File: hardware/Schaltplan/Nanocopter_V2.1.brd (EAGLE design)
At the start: 142 x 100 mm, 123 parts, among them IC1 CY7C68013A-56QFNLFXC, M1A TPSQTP20SQ, M1B TPSQTP20SQ, M1C TPSQTP20SQ, M2A TPSQTP20SQ, M2B TPSQTP20SQ, M2C TPSQTP20SQ, M3A TPSQTP20SQ, M3B TPSQTP20SQ, M3C TPSQTP20SQ, M4A TPSQTP20SQ, M4B TPSQTP20SQ, M4C TPSQTP20SQ, T5 IRLML2502, T6 IRLML2502, T7 IRLML2502, T8 IRLML2502, U2 PRTR5V0U2X, U3 LM3480-3.3, X1 USBSMD, X2 53261-08, X3 53261-06, X4 53261-03, X5 53261-03, X6 53261-06

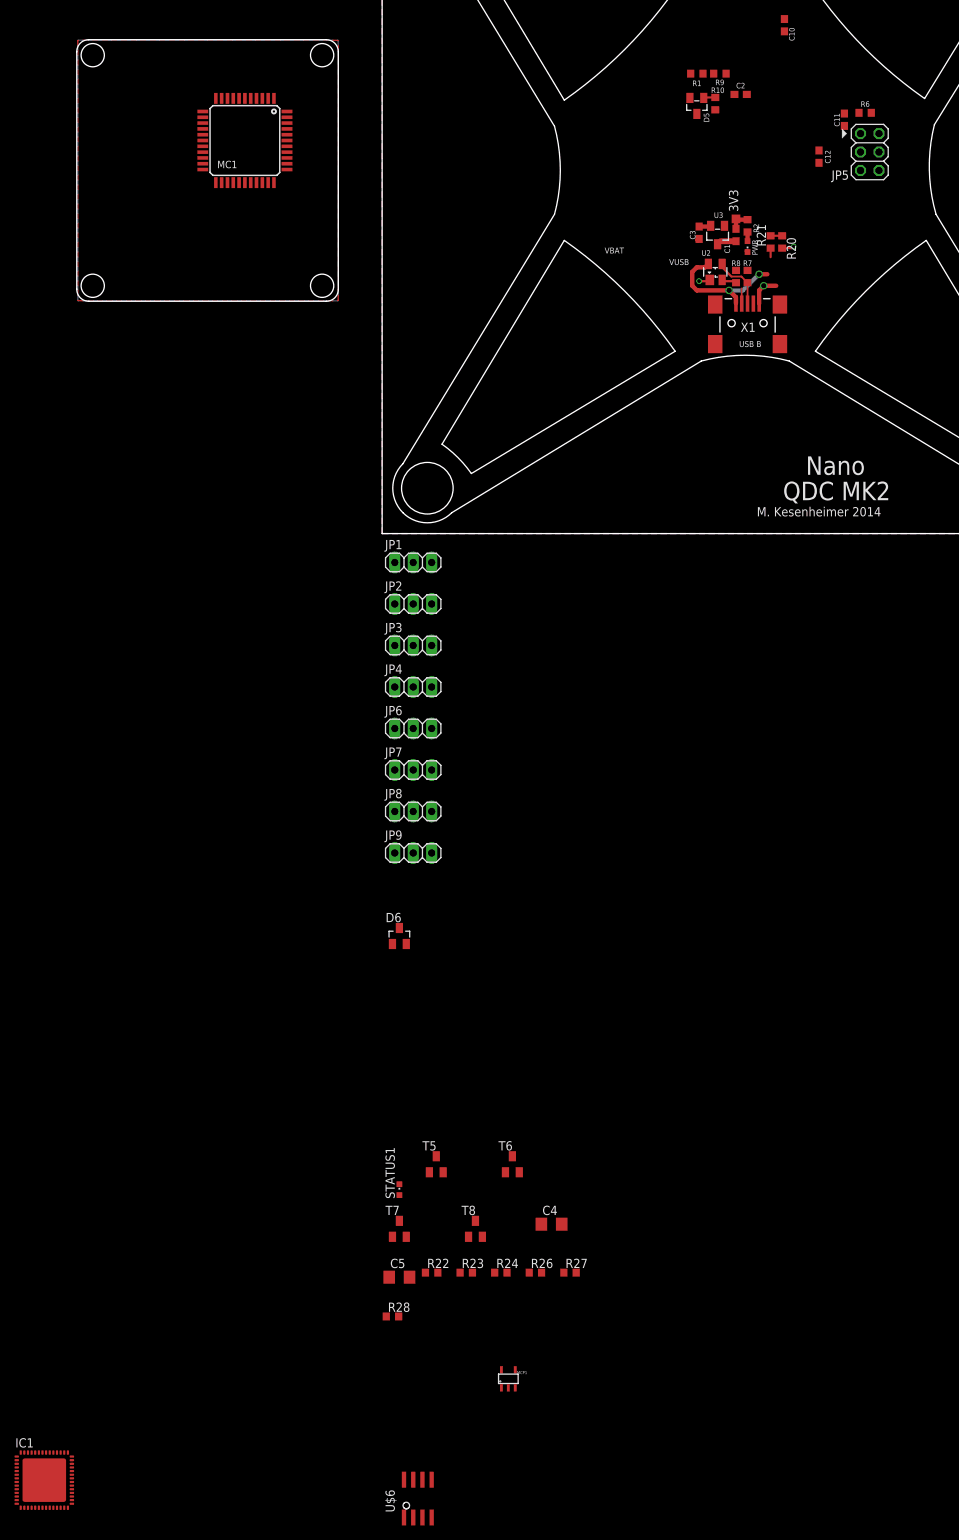
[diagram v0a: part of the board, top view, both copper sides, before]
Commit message: Dimensionen von SimpleControl aktualisiert
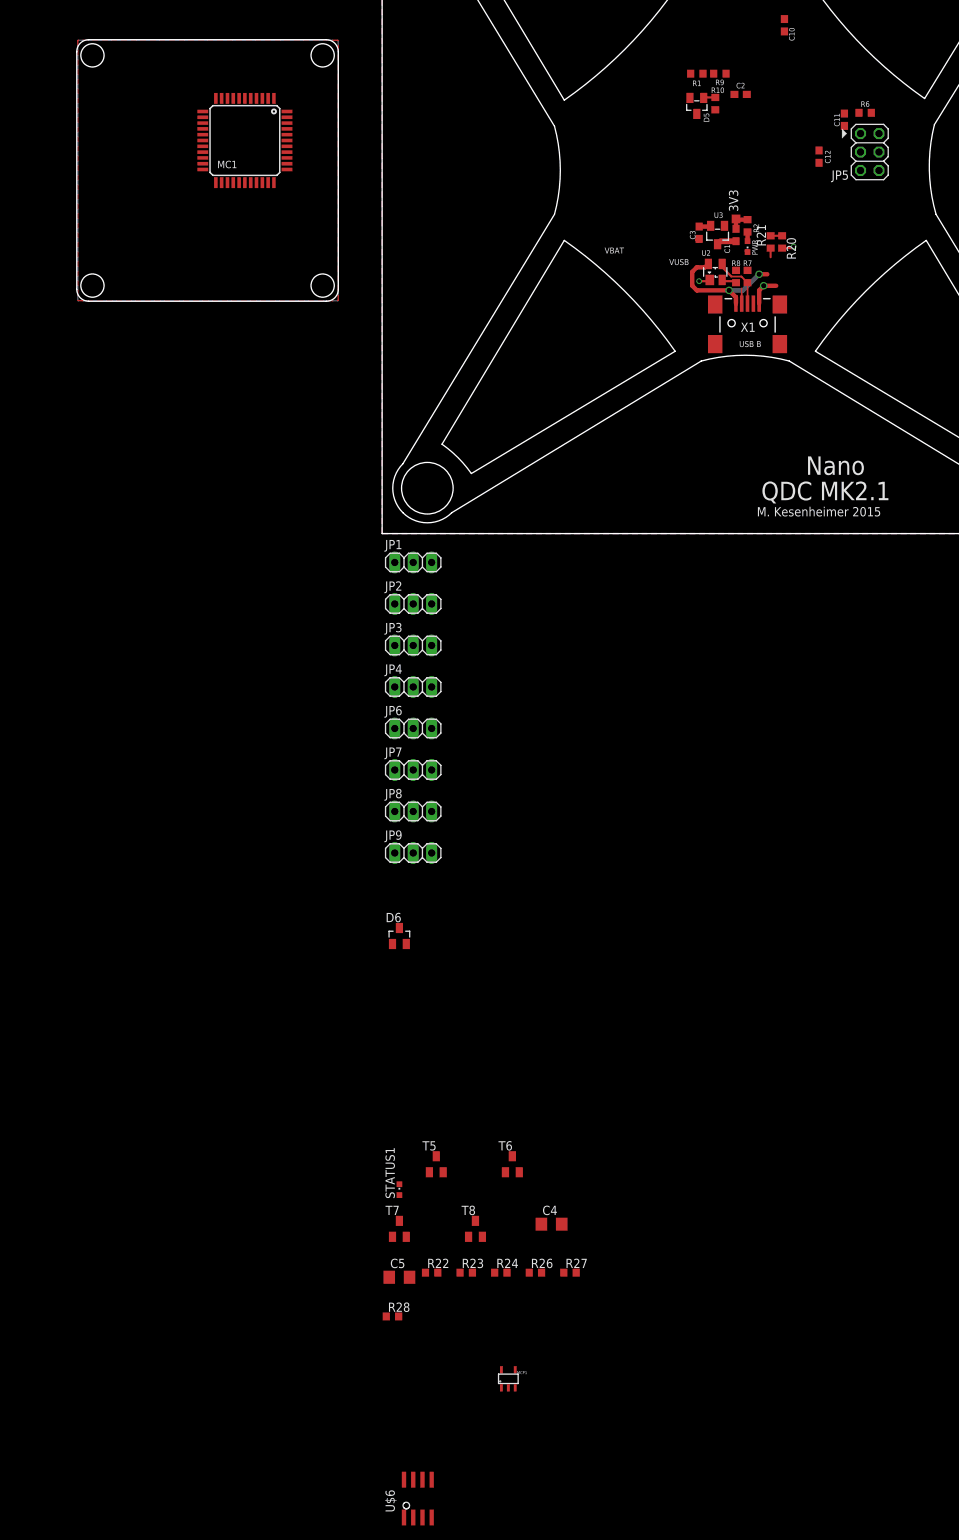
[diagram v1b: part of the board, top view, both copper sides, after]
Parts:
- removed IC1: CY7C68013A-56QFNLFXC, cypress:QFN56
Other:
- board text added: "M. Kesenheimer 2015"
- board text added: "Nano QDC MK2.1"
- board text added: "QDC MK2.1"
- board text removed: "M. Kesenheimer 2014"
- board text removed: "Nano QDC MK2"
- board text removed: "QDC MK2"
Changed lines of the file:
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@@
 <circle x="-43.7749" y="43.8052" radius="3.55" width="0.0508" layer="20"/>
 <circle x="-43.7749" y="-43.7523" radius="3.55" width="0.0508" layer="20"/>
-<text x="20.0025" y="-42.8625" size="2.54" layer="21" font="vector" rot="R180">QDC MK2</text>
-<text x="13.6525" y="-19.3675" size="2.54" layer="22" font="vector" rot="MR0">Nano QDC MK2</text>
-<text x="10.16" y="-20.955" size="1.27" layer="22" font="vector" rot="MR0">M. Kesenheimer 2014</text>
-<text x="1.5875" y="-47.625" size="1.27" layer="21" font="vector">M. Kesenheimer 2014</text>
+<text x="20.0025" y="-42.8625" size="2.54" layer="21" font="vector" rot="R180">QDC MK2.1</text>
+<text x="13.6525" y="-19.3675" size="2.54" layer="22" font="vector" rot="MR0">Nano QDC MK2.1</text>
+<text x="10.16" y="-20.955" size="1.27" layer="22" font="vector" rot="MR0">M. Kesenheimer 2015</text>
+<text x="1.5875" y="-47.625" size="1.27" layer="21" font="vector">M. Kesenheimer 2015</text>
 <text x="2.2225" y="-23.495" size="0.8128" layer="21" font="vector" rot="R180">USB B</text>
 <text x="-10.4775" y="-13.0175" size="0.8128" layer="21" font="vector">VUSB</text>
@@
 <wire x1="-57.6834" y1="-18.0086" x2="-56.0324" y2="-16.3576" width="0" layer="20" curve="90"/>
 <wire x1="-56.0324" y1="-16.3576" x2="-56.0324" y2="16.3576" width="0" layer="20"/>
-<hole x="-89.8525" y="15.875" drill="3.2"/>
-<hole x="-89.8525" y="-15.875" drill="3.2"/>
-<hole x="-58.26125" y="-15.875" drill="3.2"/>
-<hole x="-58.26125" y="15.875" drill="3.2"/>
+<hole x="-89.8906" y="15.8496" drill="3.2"/>
+<hole x="-89.8906" y="-15.8496" drill="3.2"/>
+<hole x="-58.1914" y="-15.8496" drill="3.2"/>
+<hole x="-58.1914" y="15.8496" drill="3.2"/>
+<wire x1="-92.0496" y1="-18.0086" x2="-92.0496" y2="18.0086" width="0" layer="48"/>
+<wire x1="-92.0496" y1="-18.0086" x2="-56.0324" y2="-18.0086" width="0" layer="48"/>
+<wire x1="-56.0324" y1="18.0086" x2="-56.0324" y2="-18.0086" width="0" layer="48"/>
+<wire x1="-56.0324" y1="18.0086" x2="-92.0496" y2="18.0086" width="0" layer="48"/>
+<wire x1="-92.0496" y1="18.0086" x2="-56.0324" y2="-18.0086" width="0" layer="48"/>
+<wire x1="-56.0324" y1="18.0086" x2="-92.0496" y2="-18.0086" width="0" layer="48"/>
 </plain>
 <attributes>
@@
 <element name="SJ3" library="jumper" package="SJ_2" value="" x="86.36" y="-174.3075"/>
 <element name="U$6" library="irf" package="SO8" value="IRF7321" x="-45.085" y="-182.88"/>
-<element name="IC1" library="cypress" package="QFN56" value="CY7C68013A-56QFNLFXC" x="-96.52" y="-180.34">
-<attribute name="OC_NEWARK" value="unknown" x="-96.52" y="-180.34" size="1.778" layer="27" display="off"/>
-<attribute name="MPN" value="" x="-96.52" y="-180.34" size="1.778" layer="27" display="off"/>
-<attribute name="MF" value="" x="-96.52" y="-180.34" size="1.778" layer="27" display="off"/>
-<attribute name="OC_FARNELL" value="unknown" x="-96.52" y="-180.34" size="1.778" layer="27" display="off"/>
-</element>
 </elements>
 <signals>

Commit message: Arbeit an den Dimensionen
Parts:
- moved MC1 171.3 mm to (92.4, -53.7)
- moved C10 78.6 mm to (-7.94, -57.5)
- moved C1 72.9 mm to (-17.1, -80.0)
- moved C11 72.9 mm to (-2.22, -64.1)
- moved C12 72.9 mm to (-5.71, -69.2)
- moved C17 72.9 mm to (25.7, -75.2)
- moved C2 72.9 mm to (-16.5, -60.6)
- moved C21 72.9 mm to (28.6, -72.1)
- moved D5 72.9 mm to (-22.5, -62.2)
- moved JP5 72.9 mm to (1.27, -68.6)
- moved MPU9150 72.9 mm to (24.8, -71.4)
- moved PWR 72.9 mm to (-15.6, -81.6)
- moved R1 72.9 mm to (-22.5, -57.8)
- moved R10 72.9 mm to (-20.0, -61.9)
- moved R20 72.9 mm to (-10.8, -81.0)
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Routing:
- net +3V3: track 32.1 -> 29.1 mm
- net GND: track 30.5 -> 28.6 mm, vias 6 -> 5
- net N$6: track 1.63 -> 0.14 mm
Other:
- board size 142 x 100 mm -> 440.1 x 448 mm
